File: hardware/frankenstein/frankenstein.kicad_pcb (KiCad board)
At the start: 2 copper layers, 100 x 99.9 mm, 231 parts, among them J351 J351, M200 CONN_1, M201 CONN_1, M202 CONN_1, P1 CONN_3, P104 CONN_4, P2 CONN_10X2, P201 CONN_10X2, P202 CONN_3, P203 CONN_2, P204 CONN_1, P205 CONN_1, P208 CONN_6, P209 CONN_6, P3 CONN_16, P351 CONN_5X2, P352 MICRO-SDCARD-CONNECTOR-330006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, P353 CONN_10X2, P356 CONN_1, P4 CONN_1, P472 CONN_2, P5 CONN_1, P51 CONN_4X2, P52 CONN_10X2, P53 CONN_2, P54 CONN_5X2, P55 CONN_6, P56 CONN_6, P57 CONN_6, P58 CONN_6, Q1 OVP_DRIVER, Q10 OVP_DRIVER, Q11 OVP_DRIVER, Q12 OVP_DRIVER, Q2 OVP_DRIVER, Q3 OVP_DRIVER, Q4 OVP_DRIVER, Q5 OVP_DRIVER, Q6 OVP_DRIVER, Q7 OVP_DRIVER, Q8 OVP_DRIVER, Q9 OVP_DRIVER, U101 MAX9926/9927, U201 LMV324IDR, U202 LMV324IDR, U203 LMV324IDR, U351 FT232RL, U471 SN65HVD230

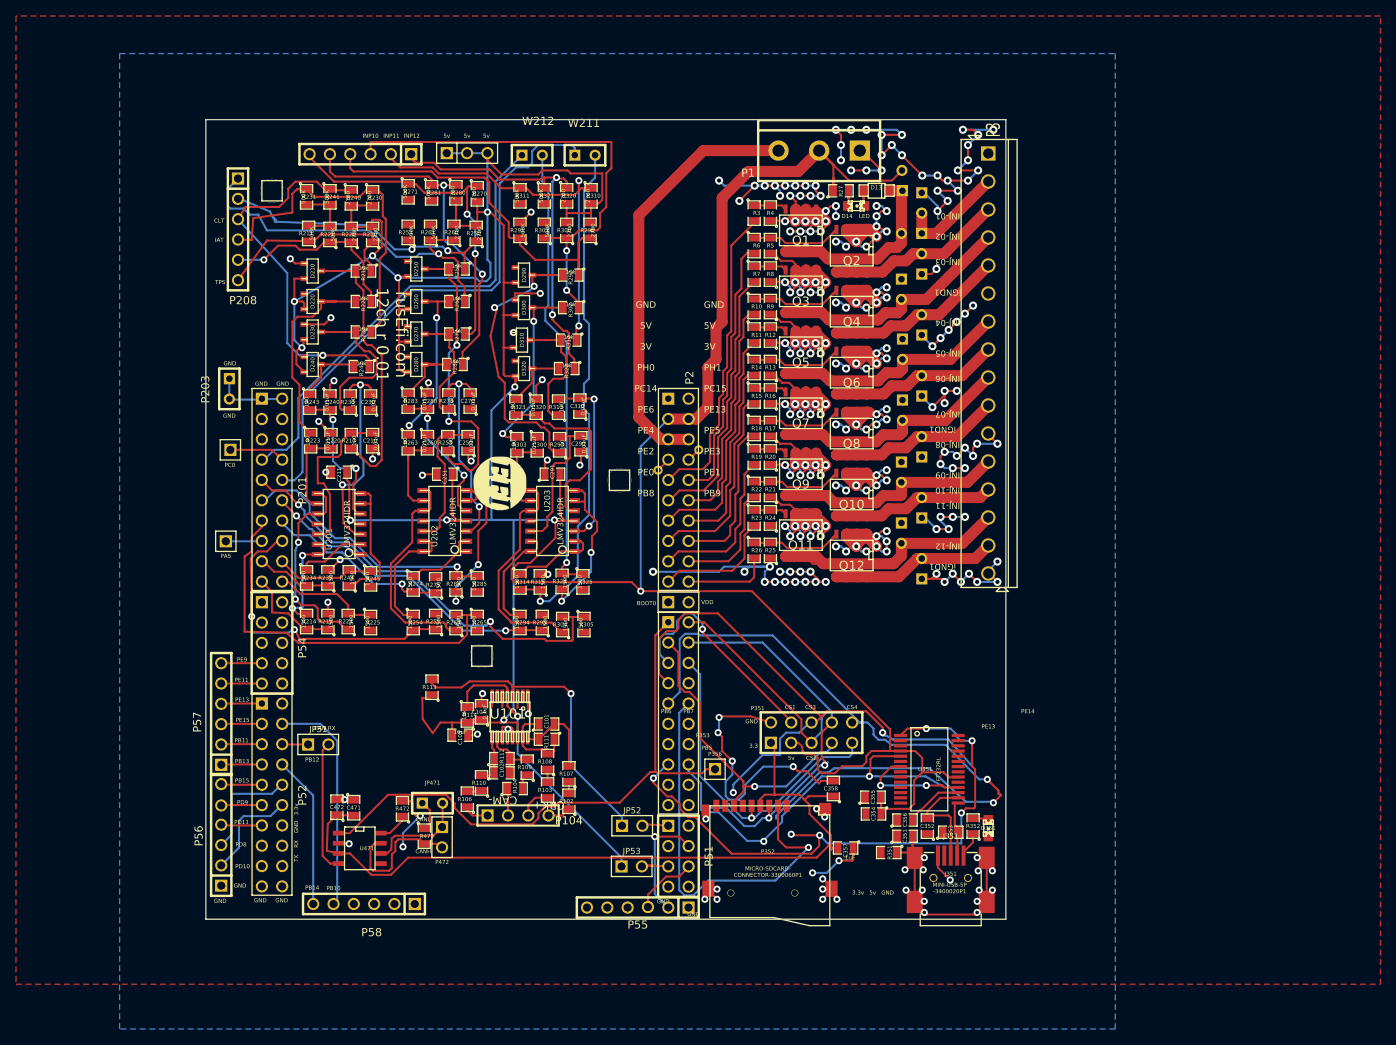
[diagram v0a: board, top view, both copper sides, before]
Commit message: 
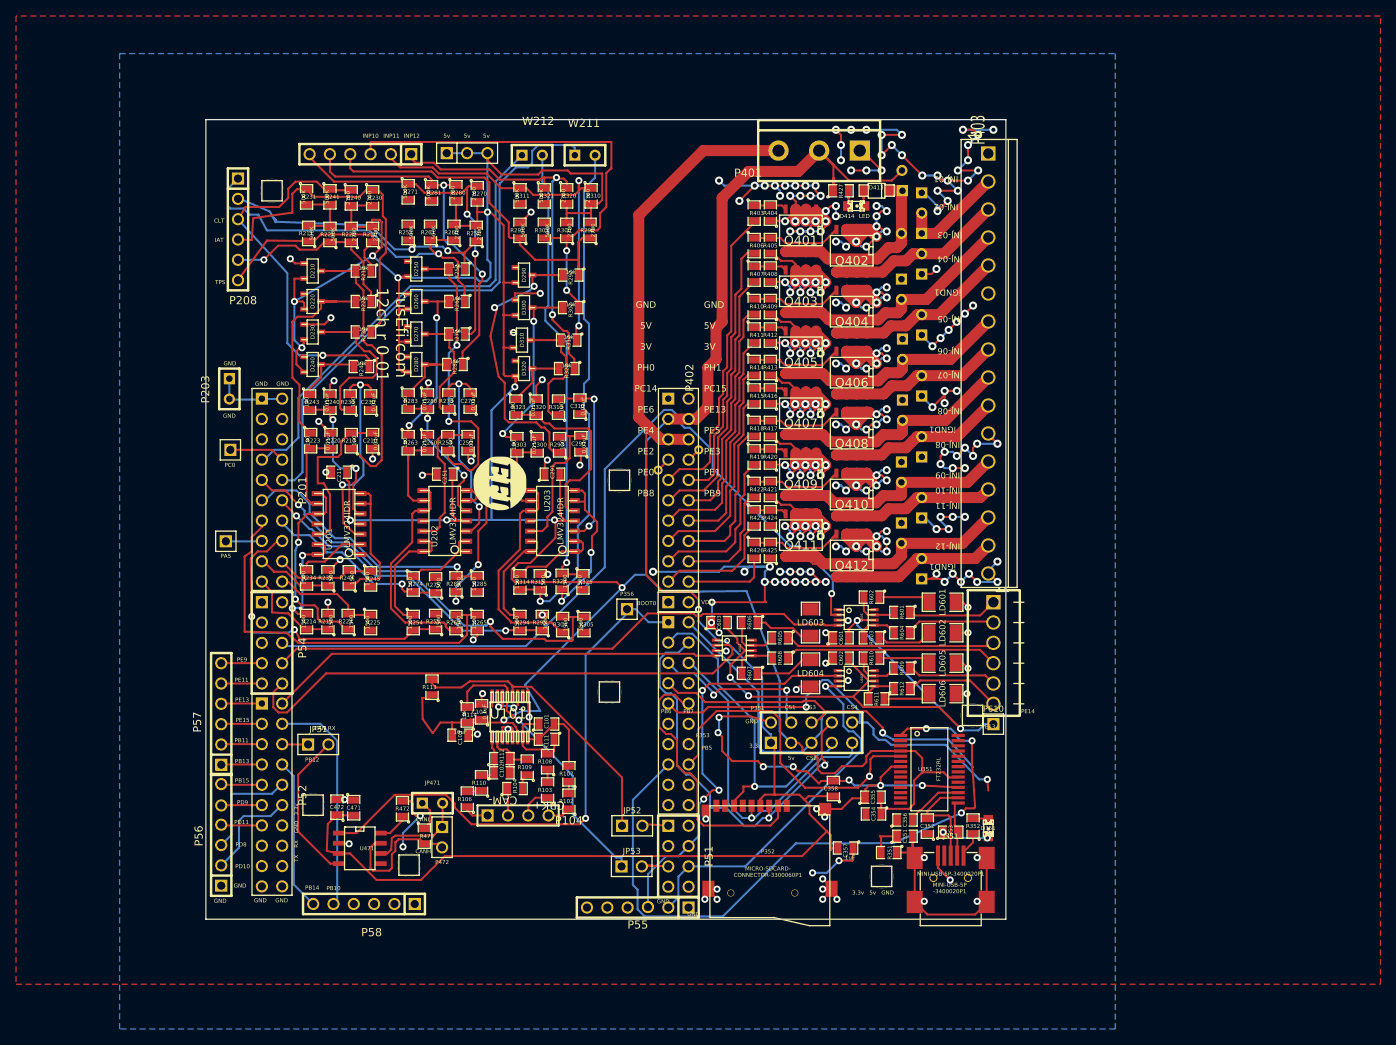
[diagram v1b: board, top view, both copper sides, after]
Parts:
- added C601: 0.1uF, SM0805, F.Cu at (199.4, 156.8)
- added C602: 0.1uF, SM0805, F.Cu at (199.4, 159.4)
- added C603: 0.1uF, SM0805, F.Cu at (184.2, 154.9)
- added G601: LOGO, LOGO_F, B.Cu at (184.3, 158.9)
- added LD601: LED, SM1206, F.Cu at (212.1, 152.4)
- added LD602: LED, SM1206, F.Cu at (212.1, 156.2)
- added LD603: LED, SM1206, F.Cu at (195.6, 154.9)
- added LD604: LED, SM1206, F.Cu at (195.6, 161.3)
- added LD605: LED, SM1206, F.Cu at (212.1, 160.0)
- added LD606: LED, SM1206, F.Cu at (212.1, 163.8)
- added M351: CONN_1, PIN_ARRAY_1, F.Cu at (204.5, 186.7)
- added M352: CONN_1, PIN_ARRAY_1, F.Cu at (215.8, 166.5)
- added M470: CONN_1, PIN_ARRAY_1, F.Cu at (133.4, 177.8)
- added M471: CONN_1, PIN_ARRAY_1, F.Cu at (145.4, 185.3)
- added P603: CONN_6, OSTVN06A150, F.Cu at (218.4, 158.8)
- added P610: CONN_1, PIN_ARRAY_1, F.Cu at (218.4, 167.6)
- added R601: 100, SM0805, F.Cu at (207.0, 153.7)
- added R602: 2700, SM0805, F.Cu at (203.2, 151.8)
- added R603: 2700, SM0805, F.Cu at (203.2, 156.8)
- added R604: 100, SM0805, F.Cu at (207.0, 156.2)
- added R605: 100, SM0805, F.Cu at (191.8, 156.8)
- added R606: 2700, SM0805, F.Cu at (188.0, 154.9)
- added R607: 2700, SM0805, F.Cu at (188.0, 161.3)
- added R608: 100, SM0805, F.Cu at (191.8, 159.4)
- added R609: 100, SM0805, F.Cu at (207.0, 160.7)
- added R610: 2700, SM0805, F.Cu at (203.2, 159.4)
- added R611: 2700, SM0805, F.Cu at (203.8, 164.5)
- added R612: 100, SM0805, F.Cu at (207.0, 163.2)
- added U601: TC4427AVOA, msoic-8, F.Cu at (201.3, 154.3)
- added U602: TC4427AVOA, msoic-8, F.Cu at (186.1, 158.1)
- added U603: TC4427AVOA, msoic-8, F.Cu at (201.3, 161.9)
- J351: value J351 -> MINI-USB-5P-3400020P1
- moved P356 22.8 mm to (172.6, 153.3)
- moved M200 16.6 mm to (170.4, 163.6)
- renumbered D1 to D401, D2 to D402, D3 to D403, D4 to D404, D5 to D405, D6 to D406, D7 to D407, D8 to D408, D9 to D409, D10 to D410, D11 to D411, D12 to D412, D13 to D413, D14 to D414, P1 to P401, P2 to P402, P3 to P403, P4 to P404, P5 to P405, Q1 to Q401, Q2 to Q402, Q3 to Q403, Q4 to Q404, Q5 to Q405, Q6 to Q406, Q7 to Q407, Q8 to Q408, Q9 to Q409, Q10 to Q410, Q11 to Q411, Q12 to Q412, R1 to R401, R2 to R402, R3 to R403, R4 to R404, R5 to R405, R6 to R406, R7 to R407, R8 to R408, R9 to R409, R10 to R410, R11 to R411, R12 to R412, R13 to R413, R14 to R414, R15 to R415, R16 to R416, R17 to R417, R18 to R418, R19 to R419, R20 to R420, R21 to R421, R22 to R422, R23 to R423, R24 to R424, R25 to R425, R26 to R426, R27 to R427
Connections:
- net F-0000103 renamed F-000085
- net F-0000146 renamed F-0000112
- net F-0000184 renamed F-0000158
- net F-0000185 renamed F-0000152
- net F-0000186 renamed F-0000151
- net F-0000187 renamed F-0000157
- net F-0000188 renamed F-0000160
- net F-0000190 renamed F-0000156
- net F-0000191 renamed F-0000149
- net F-0000192 renamed F-0000153
- net F-0000193 renamed F-0000161
- net F-0000195 renamed F-0000159
- net F-0000196 renamed F-0000150
- net F-0000197 renamed F-0000162
- net F-000089 renamed F-000083
- net F-000095 renamed F-000081
- C101 pad 1: F-0000145 -> F-0000111
- C102 pad 1: F-0000147 -> F-0000113
- C102 pad 2: F-0000148 -> F-0000114
- C352 pad 2: F-0000120 -> F-000088
- D351 pad 1: F-000088 -> F-000082
- D413 pad 1: F-0000194 -> F-0000154
- D414 pad 2: F-0000194 -> F-0000154
- J351 pad 3: F-0000120 -> F-000088
- J351 pad 4: F-0000100 -> (no net)
- JP471 pad 1: F-0000155 -> F-0000120
- P352 pad 1: F-0000119 -> (no net)
- P352 pad 8: F-0000118 -> (no net)
- P352 pad 9: F-0000117 -> (no net)
- P353 pad 11: F-000094 -> (no net)
- P353 pad 12: F-000098 -> (no net)
- P353 pad 13: F-000093 -> (no net)
- P353 pad 14: F-000097 -> (no net)
- P353 pad 17: F-000092 -> (no net)
- P353 pad 18: F-000096 -> (no net)
- P353 pad 19: F-000091 -> (no net)
- P353 pad 20: F-000090 -> (no net)
- P353 pad 8: F-000099 -> (no net)
- P401 pad 3: /3V -> /3.3V
- P402 pad 5: /3V -> /3.3V
- P402 pad 6: /3V -> /3.3V
- P51 pad 4: /PC9 -> /H_IN6
- P51 pad 6: /PC7 -> /H_IN5
- P52 pad 2: (no net) -> /H_IN4
- P54 pad 10: (no net) -> /H_IN2
- P54 pad 6: (no net) -> /H_IN3
- P54 pad 8: (no net) -> /H_IN1
- P55 pad 1: (no net) -> GND
- P55 pad 2: /PC9 -> /H_IN5
- P55 pad 3: /PC7 -> /H_IN6
- P55 pad 6: (no net) -> GND
- P58 pad 1: (no net) -> GND
- P58 pad 2: (no net) -> GND
- P58 pad 3: (no net) -> GND
- P58 pad 4: (no net) -> GND
- Q410 pad 1: F-0000189 -> F-0000155
- R102 pad 2: F-0000140 -> F-0000106
- R103 pad 2: F-0000144 -> F-0000110
- R104 pad 2: F-0000141 -> F-0000107
- R106 pad 2: F-0000143 -> F-0000109
- R107 pad 1: F-0000140 -> F-0000106
- R108 pad 1: F-0000144 -> F-0000110
- R108 pad 2: F-0000145 -> F-0000111
- R109 pad 1: F-0000141 -> F-0000107
- R109 pad 2: F-0000148 -> F-0000114
- R110 pad 1: F-0000143 -> F-0000109
- R110 pad 2: F-0000147 -> F-0000113
- R111 pad 1: F-0000145 -> F-0000111
- R112 pad 1: F-0000147 -> F-0000113
- R112 pad 2: F-0000148 -> F-0000114
- R352 pad 2: F-000088 -> F-000082
- R421 pad 2: F-0000189 -> F-0000155
- R422 pad 1: F-0000189 -> F-0000155
- R472 pad 1: F-0000154 -> F-0000121
- R473 pad 1: F-0000155 -> F-0000120
- U101 pad 10: F-0000148 -> F-0000114
- U101 pad 15: F-0000145 -> F-0000111
- U101 pad 9: F-0000147 -> F-0000113
- U351 pad 10: F-0000109 -> (no net)
- U351 pad 11: F-0000108 -> (no net)
- U351 pad 12: F-0000101 -> (no net)
- U351 pad 13: F-0000106 -> (no net)
- U351 pad 14: F-0000104 -> (no net)
- U351 pad 16: F-0000120 -> F-000088
- U351 pad 19: F-0000113 -> (no net)
- U351 pad 2: F-0000116 -> (no net)
- U351 pad 22: F-0000107 -> (no net)
- U351 pad 23: F-0000105 -> (no net)
- U351 pad 27: F-0000102 -> (no net)
- U351 pad 28: F-0000115 -> (no net)
- U351 pad 3: F-0000114 -> (no net)
- U351 pad 6: F-0000111 -> (no net)
- U351 pad 9: F-0000110 -> (no net)
- U471 pad 8: F-0000154 -> F-0000121
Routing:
- net /H_IN3: track 0.00 -> 104.2 mm, vias 0 -> 1
- net /3.3V: track 99.8 -> 202.6 mm, vias 0 -> 1
- net /VP: track 0.00 -> 77.6 mm, vias 0 -> 4
- net /H_IN1: track 0.00 -> 72.8 mm
- net /H_IN2: track 0.00 -> 67.1 mm
- net /H_IN4: track 0.00 -> 56.9 mm
- net /3V: track 53.4 -> 0.00 mm
- net GND: track 625.9 -> 677.0 mm, vias 242 -> 262
- net /H_IN6: track 0.00 -> 50.7 mm, vias 0 -> 3
- net /H_IN5: track 0.00 -> 45.7 mm, vias 0 -> 1
- net /CS4: track 92.2 -> 51.5 mm
- net /CS3: track 73.8 -> 46.6 mm, vias 2 -> 1
- net /HL4: track 0.00 -> 26.8 mm
- net /HL3: track 0.00 -> 26.3 mm
- net /CS_SD_MODULE: track 51.2 -> 34.3 mm, vias 1 -> 0
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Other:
- net class Default: clearance 0.2032 -> 0.1524
- rule trace_clearance: 0.2032 -> 0.1524
- board text added: "HI-LO1"
- board text added: "HI-LO2"
- board text added: "HI-LO3"
- board text added: "HI-LO4"
- board text added: "HI-LO5"
- board text added: "HI-LO6"
- board text added: "VP"
- board text added: "for RUSEFI.com"
- board text added: "https://code.google.com/p/daecu/ R.01"

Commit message: getting closer to RC2
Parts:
- removed G200: LOGO, LOGO
- removed G202: LOGO, LOGO_F
- added M401: CONN_1, 1pin, F.Cu at (210.8, 95.2)
- M200, M201, M202: footprint PIN_ARRAY_1 -> 1pin
- P204, P205: moved to B.Cu
- P208, P209: footprint PIN_ARRAY-6X1 -> 6_screw_term_.1in
- moved M200 83.6 mm to (123.2, 94.6)
- moved W211 63.3 mm to (133.3, 149.9)
- moved M201 47.9 mm to (123.2, 148.6)
- moved M202 43.1 mm to (178.4, 94.6)
- moved R224 42.7 mm to (124.5, 114.3), turned to 180 degrees
- moved G201 41.6 mm to (176.4, 114.2), turned to 90 degrees
- moved R225 41.4 mm to (124.5, 116.8), turned to 0 degrees
- moved R314 41.3 mm to (180.3, 114.3), turned to 0 degrees
- moved R264 41.1 mm to (145.4, 114.3), turned to 180 degrees
- moved R304 40.9 mm to (166.4, 114.3), turned to 180 degrees
- moved P203 40.7 mm to (149.9, 95.2), turned to 180 degrees
- moved R265 39.0 mm to (145.4, 116.8), turned to 0 degrees
- moved R305 38.4 mm to (166.4, 116.8), turned to 0 degrees
- moved R274 38.3 mm to (159.4, 114.3), turned to 0 degrees
- moved R315 37.9 mm to (180.3, 116.8), turned to 180 degrees
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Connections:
- net F-0000106 renamed F-000020
- net F-0000111 renamed F-000025
- net F-0000113 renamed F-000027
- net F-0000114 renamed F-000028
- net F-000038 renamed F-000065
- net F-000044 renamed F-000073
- net F-000046 renamed F-000072
- net F-000047 renamed F-000074
- net F-000048 renamed F-000075
- net F-000049 renamed F-000076
- net F-000050 renamed F-000078
- net F-000052 renamed F-000077
- net F-000053 renamed F-000079
- C101 pad 2: F-0000112 -> F-000026
- C210 pad 2: F-000061 -> F-000088
- C220 pad 2: F-000059 -> F-000086
- C230 pad 2: F-000056 -> F-000083
- C240 pad 2: F-000055 -> F-000082
- C260 pad 2: F-000062 -> F-000089
- C270 pad 2: F-000057 -> F-000084
- C280 pad 2: F-000058 -> F-000085
- C300 pad 2: F-000040 -> F-000067
- C310 pad 2: F-000043 -> F-000070
- C320 pad 2: F-000045 -> F-000071
- C351 pad 2: F-000083 -> F-0000110
- C352 pad 2: F-000088 -> F-0000115
- C353 pad 2: F-000081 -> F-0000108
- C356 pad 2: F-000085 -> F-0000112
- D220 pad 2: F-000060 -> F-000087
- D230 pad 2: F-000066 -> F-000093
- D240 pad 2: F-000064 -> F-000091
- D250 pad 2: F-000039 -> F-000066
- D270 pad 2: F-000032 -> F-000059
- D280 pad 2: F-000029 -> F-000056
- D290 pad 2: F-000035 -> F-000062
- D300 pad 2: F-000034 -> F-000061
- D351 pad 1: F-000082 -> F-0000109
- D413 pad 1: F-0000154 -> F-0000149
- D414 pad 1: F-0000153 -> F-0000147
- D414 pad 2: F-0000154 -> F-0000149
- J351 pad 1: F-000080 -> F-0000107
- J351 pad 2: F-000081 -> F-0000108
- J351 pad 3: F-000088 -> F-0000115
- J351 pad 6: F-000083 -> F-0000110
- JP471 pad 1: F-0000120 -> F-0000161
- P201 pad 10: /OUT11 -> /OUT6
- P201 pad 11: /OUT8 -> /OUT1
- P201 pad 12: /OUT9 -> /OUT5
- P201 pad 13: /OUT6 -> /OUT2
- P201 pad 14: /OUT7 -> /OUT8
- P201 pad 16: /OUT5 -> /OUT7
- P201 pad 17: /OUT3 -> /OUT10
- P201 pad 18: /OUT4 -> /OUT9
- P201 pad 19: /OUT1 -> /OUT12
- P201 pad 20: /OUT2 -> /OUT11
- P201 pad 7: /OUT12 -> /OUT4
- P201 pad 9: /OUT10 -> /OUT3
- P208 pad 1: /INP6 -> /INP1
- P208 pad 2: /INP5 -> /INP2
- P208 pad 3: /INP4 -> /INP3
- P208 pad 4: /INP3 -> /INP4
- P208 pad 5: /INP2 -> /INP5
- P208 pad 6: /INP1 -> /INP6
- P209 pad 1: /INP12 -> /INP7
- P209 pad 2: /INP11 -> /INP8
- P209 pad 3: /INP10 -> /INP9
- P209 pad 4: /INP9 -> /INP10
- P209 pad 5: /INP8 -> /INP11
- P209 pad 6: /INP7 -> /INP12
- P401 pad 2: /5V -> /3.3V
- P401 pad 3: /3.3V -> /5V
- Q401 pad 1: F-0000159 -> F-0000151
- Q402 pad 1: F-0000151 -> F-0000146
- Q403 pad 1: F-0000158 -> F-0000153
- Q404 pad 1: F-0000152 -> F-0000144
- Q405 pad 1: F-0000157 -> F-0000152
- Q406 pad 1: F-0000150 -> F-0000145
- Q407 pad 1: F-0000161 -> F-0000155
- Q408 pad 1: F-0000149 -> F-0000143
- Q409 pad 1: F-0000160 -> F-0000154
- Q410 pad 1: F-0000155 -> F-0000148
- Q411 pad 1: F-0000162 -> F-0000156
- Q412 pad 1: F-0000156 -> F-0000150
- R103 pad 2: F-0000110 -> F-000024
- R104 pad 2: F-0000107 -> F-000021
- R106 pad 2: F-0000109 -> F-000023
- R107 pad 2: F-0000112 -> F-000026
- R108 pad 1: F-0000110 -> F-000024
- R109 pad 1: F-0000107 -> F-000021
- R110 pad 1: F-0000109 -> F-000023
- R111 pad 2: F-0000112 -> F-000026
- R213 pad 2: F-000061 -> F-000088
- R214 pad 1: F-000030 -> F-000057
- R222 pad 2: F-000060 -> F-000087
- R223 pad 1: F-000060 -> F-000087
- R223 pad 2: F-000059 -> F-000086
- R224 pad 1: F-000031 -> F-000058
- R232 pad 2: F-000066 -> F-000093
- R233 pad 1: F-000066 -> F-000093
- R233 pad 2: F-000056 -> F-000083
- R234 pad 1: F-000067 -> F-000094
- R242 pad 2: F-000064 -> F-000091
- R243 pad 1: F-000064 -> F-000091
- R243 pad 2: F-000055 -> F-000082
- R244 pad 1: F-000033 -> F-000060
- R252 pad 2: F-000039 -> F-000066
- R253 pad 1: F-000039 -> F-000066
- R263 pad 2: F-000062 -> F-000089
- R264 pad 1: F-000054 -> F-000081
- R272 pad 2: F-000032 -> F-000059
- R273 pad 1: F-000032 -> F-000059
- R273 pad 2: F-000057 -> F-000084
- R274 pad 1: F-000051 -> F-000080
- R282 pad 2: F-000029 -> F-000056
- R283 pad 1: F-000029 -> F-000056
- R283 pad 2: F-000058 -> F-000085
- R284 pad 1: F-000063 -> F-000090
- R292 pad 2: F-000035 -> F-000062
- R293 pad 1: F-000035 -> F-000062
- R294 pad 1: F-000037 -> F-000064
- R302 pad 2: F-000034 -> F-000061
- R303 pad 1: F-000034 -> F-000061
- R303 pad 2: F-000040 -> F-000067
- R304 pad 1: F-000036 -> F-000063
- R313 pad 2: F-000043 -> F-000070
- R314 pad 1: F-000042 -> F-000068
- R323 pad 2: F-000045 -> F-000071
- R324 pad 1: F-000041 -> F-000069
- R351 pad 1: F-000083 -> F-0000110
- R352 pad 1: F-000080 -> F-0000107
- R352 pad 2: F-000082 -> F-0000109
- R403 pad 1: F-0000159 -> F-0000151
- R404 pad 2: F-0000159 -> F-0000151
- R405 pad 2: F-0000151 -> F-0000146
- R406 pad 1: F-0000151 -> F-0000146
- R407 pad 1: F-0000158 -> F-0000153
- R408 pad 2: F-0000158 -> F-0000153
- R409 pad 2: F-0000152 -> F-0000144
- R410 pad 1: F-0000152 -> F-0000144
- R411 pad 1: F-0000157 -> F-0000152
- R412 pad 2: F-0000157 -> F-0000152
- R413 pad 2: F-0000150 -> F-0000145
- R414 pad 1: F-0000150 -> F-0000145
- R415 pad 1: F-0000161 -> F-0000155
- R416 pad 2: F-0000161 -> F-0000155
- R417 pad 2: F-0000149 -> F-0000143
- R418 pad 1: F-0000149 -> F-0000143
- R419 pad 1: F-0000160 -> F-0000154
- R420 pad 2: F-0000160 -> F-0000154
- R421 pad 2: F-0000155 -> F-0000148
- R422 pad 1: F-0000155 -> F-0000148
- R423 pad 1: F-0000162 -> F-0000156
- R424 pad 2: F-0000162 -> F-0000156
- R425 pad 2: F-0000156 -> F-0000150
- R426 pad 1: F-0000156 -> F-0000150
- R427 pad 2: F-0000153 -> F-0000147
- R472 pad 1: F-0000121 -> F-0000162
- R473 pad 1: F-0000120 -> F-0000161
- U101 pad 16: F-0000112 -> F-000026
- U201 pad 1: F-000067 -> F-000060
- U201 pad 10: F-000031 -> F-000086
- U201 pad 12: F-000061 -> F-000088
- U201 pad 13: F-000030 -> F-000057
- U201 pad 14: F-000030 -> F-000057
- U201 pad 2: F-000067 -> F-000060
- U201 pad 3: F-000056 -> F-000082
- U201 pad 5: F-000055 -> F-000083
- U201 pad 6: F-000033 -> F-000094
- U201 pad 7: F-000033 -> F-000094
- U201 pad 8: F-000031 -> F-000058
- U201 pad 9: F-000059 -> F-000058
- U202 pad 1: F-000051 -> F-000090
- U202 pad 10: F-000054 -> F-000089
- U202 pad 2: F-000051 -> F-000090
- U202 pad 3: F-000057 -> F-000085
- U202 pad 5: F-000058 -> F-000084
- U202 pad 6: F-000063 -> F-000080
- U202 pad 7: F-000063 -> F-000080
- U202 pad 8: F-000054 -> F-000081
- U202 pad 9: F-000062 -> F-000081
- U203 pad 1: F-000042 -> F-000069
- U203 pad 10: F-000036 -> F-000067
- U203 pad 13: F-000037 -> F-000064
- U203 pad 14: F-000037 -> F-000064
- U203 pad 2: F-000042 -> F-000069
- U203 pad 3: F-000043 -> F-000071
- U203 pad 5: F-000045 -> F-000070
- U203 pad 6: F-000041 -> F-000068
- U203 pad 7: F-000041 -> F-000068
- U203 pad 8: F-000036 -> F-000063
- U203 pad 9: F-000040 -> F-000063
- U351 pad 15: F-000081 -> F-0000108
- U351 pad 16: F-000088 -> F-0000115
- U351 pad 17: F-000085 -> F-0000112
- U471 pad 8: F-0000121 -> F-0000162
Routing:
- net /OUT11: track 68.5 -> 2.59 mm
- net /INP10: track 60.1 -> 11.5 mm, vias 2 -> 0
- net /5V: track 475.1 -> 432.3 mm, vias 11 -> 3
- net GND: track 677.0 -> 636.1 mm, vias 262 -> 267
- net F-000035: track 37.4 -> 0.00 mm, vias 2 -> 0
- net F-000039: track 37.1 -> 0.00 mm, vias 2 -> 0
- net F-000075: track 56.8 -> 20.7 mm, vias 1 -> 0
- net F-0000110: track 1.65 -> 37.5 mm, vias 0 -> 4
- net /SPI_SCK: track 42.4 -> 78.1 mm, vias 1 -> 3
- net /INP4: track 47.9 -> 12.8 mm, vias 1 -> 0
- net /INP11: track 49.8 -> 14.9 mm, vias 2 -> 0
- net /INP8: track 45.6 -> 11.3 mm, vias 2 -> 0
- net /INP9: track 44.8 -> 10.6 mm
- net /INP12: track 49.9 -> 16.3 mm, vias 2 -> 0
- net /INP3: track 43.0 -> 10.5 mm
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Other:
- net class Default: clearance 0.1524 -> 0.2032
- rule trace_clearance: 0.1524 -> 0.2032
- board text added: "5V 3V GND"
- board text added: "BAT"
- board text added: "CLT 1K TO 10K"
- board text added: "Frankenstein 0.1"
- board text added: "GND VDD GND PC1 PC3 PA1 PA5 PA7 PC5 PB1"
- board text added: "GND VDD NRST PC0 PC2 PA0 PA2 PA4 PA6 PC4"
- board text added: "IAT 1K TO 10K"
- board text added: "INP1"
- board text added: "INP2"
- board text added: "INP3"
- board text added: "INP4"
- board text added: "INP5"
- board text added: "INP6"
- board text added: "INP7"
- board text added: "INP8"
- board text added: "INP9"
- board text added: "TPS 1K TO 10K"
- board text added: "http://code.google.com/p/daecu/ for rusEFI R.01"
- board text removed: "CLT"
- board text removed: "IAT"
- board text removed: "TPS"
